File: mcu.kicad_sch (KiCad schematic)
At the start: 50 parts, among them IC3 RP2040, U1 W25Q64JVSSIQ, Y1 ABM3B-12.000MHZ-10-1-U-T

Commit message: reannotate
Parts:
- renumbered TP30 to TP28, TP31 to TP29, TP32 to TP30, TP33 to TP31, TP34 to TP32, TP37 to TP33, TP50 to TP34, TP51 to TP35, TP35 to TP36, TP36 to TP37
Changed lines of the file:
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@@
   (symbol (lib_id "Connector:TestPoint_Small") (at 198.12 133.35 0) (unit 1)
     (in_bom yes) (on_board yes) (dnp no)
-    (property "Reference" "TP33" (at 198.755 132.08 0)
+    (property "Reference" "TP31" (at 198.755 132.08 0)
       (effects (font (size 1.27 1.27)) (justify left) hide)
     )
@@
       (project "gkos_pebble"
         (path "/ab6fff6e-44fa-4992-ab9d-8d9a7df4367d/b094ad32-9f85-443d-ad4d-e6b703944261"
-          (reference "TP33") (unit 1)
+          (reference "TP31") (unit 1)
         )
       )
@@
   (symbol (lib_id "Connector:TestPoint_Small") (at 198.12 156.21 0) (unit 1)
     (in_bom yes) (on_board yes) (dnp no)
-    (property "Reference" "TP35" (at 198.755 154.94 0)
+    (property "Reference" "TP36" (at 198.755 154.94 0)
       (effects (font (size 1.27 1.27)) (justify left) hide)
     )
@@
       (project "gkos_pebble"
         (path "/ab6fff6e-44fa-4992-ab9d-8d9a7df4367d/b094ad32-9f85-443d-ad4d-e6b703944261"
-          (reference "TP35") (unit 1)
+          (reference "TP36") (unit 1)
         )
       )
@@
   (symbol (lib_id "Connector:TestPoint_Small") (at 198.12 148.59 0) (unit 1)
     (in_bom yes) (on_board yes) (dnp no)
-    (property "Reference" "TP37" (at 198.755 147.32 0)
+    (property "Reference" "TP33" (at 198.755 147.32 0)
       (effects (font (size 1.27 1.27)) (justify left) hide)
     )
@@
       (project "gkos_pebble"
         (path "/ab6fff6e-44fa-4992-ab9d-8d9a7df4367d/b094ad32-9f85-443d-ad4d-e6b703944261"
-          (reference "TP37") (unit 1)
+          (reference "TP33") (unit 1)
         )
       )
@@
   (symbol (lib_id "Connector:TestPoint_Small") (at 198.12 135.89 0) (unit 1)
     (in_bom yes) (on_board yes) (dnp no)
-    (property "Reference" "TP34" (at 198.755 134.62 0)
+    (property "Reference" "TP32" (at 198.755 134.62 0)
       (effects (font (size 1.27 1.27)) (justify left) hide)
     )
@@
       (project "gkos_pebble"
         (path "/ab6fff6e-44fa-4992-ab9d-8d9a7df4367d/b094ad32-9f85-443d-ad4d-e6b703944261"
-          (reference "TP34") (unit 1)
+          (reference "TP32") (unit 1)
         )
       )
@@
   (symbol (lib_id "Connector:TestPoint_Small") (at 162.56 57.15 0) (unit 1)
     (in_bom yes) (on_board yes) (dnp no)
-    (property "Reference" "TP32" (at 163.195 55.88 0)
+    (property "Reference" "TP30" (at 163.195 55.88 0)
       (effects (font (size 1.27 1.27)) (justify left))
     )
@@
       (project "gkos_pebble"
         (path "/ab6fff6e-44fa-4992-ab9d-8d9a7df4367d/b094ad32-9f85-443d-ad4d-e6b703944261"
-          (reference "TP32") (unit 1)
+          (reference "TP30") (unit 1)
         )
       )
@@
   (symbol (lib_id "Connector:TestPoint_Small") (at 198.12 153.67 0) (unit 1)
     (in_bom yes) (on_board yes) (dnp no)
-    (property "Reference" "TP51" (at 198.755 152.4 0)
+    (property "Reference" "TP35" (at 198.755 152.4 0)
       (effects (font (size 1.27 1.27)) (justify left) hide)
     )
@@
       (project "gkos_pebble"
         (path "/ab6fff6e-44fa-4992-ab9d-8d9a7df4367d/b094ad32-9f85-443d-ad4d-e6b703944261"
-          (reference "TP51") (unit 1)
+          (reference "TP35") (unit 1)
         )
       )
@@
   (symbol (lib_id "Connector:TestPoint_Small") (at 198.12 158.75 0) (unit 1)
     (in_bom yes) (on_board yes) (dnp no)
-    (property "Reference" "TP36" (at 198.755 157.48 0)
+    (property "Reference" "TP37" (at 198.755 157.48 0)
       (effects (font (size 1.27 1.27)) (justify left) hide)
     )
@@
       (project "gkos_pebble"
         (path "/ab6fff6e-44fa-4992-ab9d-8d9a7df4367d/b094ad32-9f85-443d-ad4d-e6b703944261"
-          (reference "TP36") (unit 1)
+          (reference "TP37") (unit 1)
         )
       )
@@
   (symbol (lib_id "Connector:TestPoint_Small") (at 53.34 135.89 0) (unit 1)
     (in_bom yes) (on_board yes) (dnp no)
-    (property "Reference" "TP30" (at 53.975 134.62 0)
+    (property "Reference" "TP28" (at 53.975 134.62 0)
       (effects (font (size 1.27 1.27)) (justify left) hide)
     )
@@
       (project "gkos_pebble"
         (path "/ab6fff6e-44fa-4992-ab9d-8d9a7df4367d/b094ad32-9f85-443d-ad4d-e6b703944261"
-          (reference "TP30") (unit 1)
+          (reference "TP28") (unit 1)
         )
       )
@@
   (symbol (lib_id "Connector:TestPoint_Small") (at 198.12 151.13 0) (unit 1)
     (in_bom yes) (on_board yes) (dnp no)
-    (property "Reference" "TP50" (at 198.755 149.86 0)
+    (property "Reference" "TP34" (at 198.755 149.86 0)
       (effects (font (size 1.27 1.27)) (justify left) hide)
     )
@@
       (project "gkos_pebble"
         (path "/ab6fff6e-44fa-4992-ab9d-8d9a7df4367d/b094ad32-9f85-443d-ad4d-e6b703944261"
-          (reference "TP50") (unit 1)
+          (reference "TP34") (unit 1)
         )
       )
@@
   (symbol (lib_id "Connector:TestPoint_Small") (at 53.34 163.83 0) (mirror x) (unit 1)
     (in_bom yes) (on_board yes) (dnp no)
-    (property "Reference" "TP31" (at 53.975 165.1 0)
+    (property "Reference" "TP29" (at 53.975 165.1 0)
       (effects (font (size 1.27 1.27)) (justify left) hide)
     )
@@
       (project "gkos_pebble"
         (path "/ab6fff6e-44fa-4992-ab9d-8d9a7df4367d/b094ad32-9f85-443d-ad4d-e6b703944261"
-          (reference "TP31") (unit 1)
-        )
-      )
+          (reference "TP29") (unit 1)
+        )
+      )

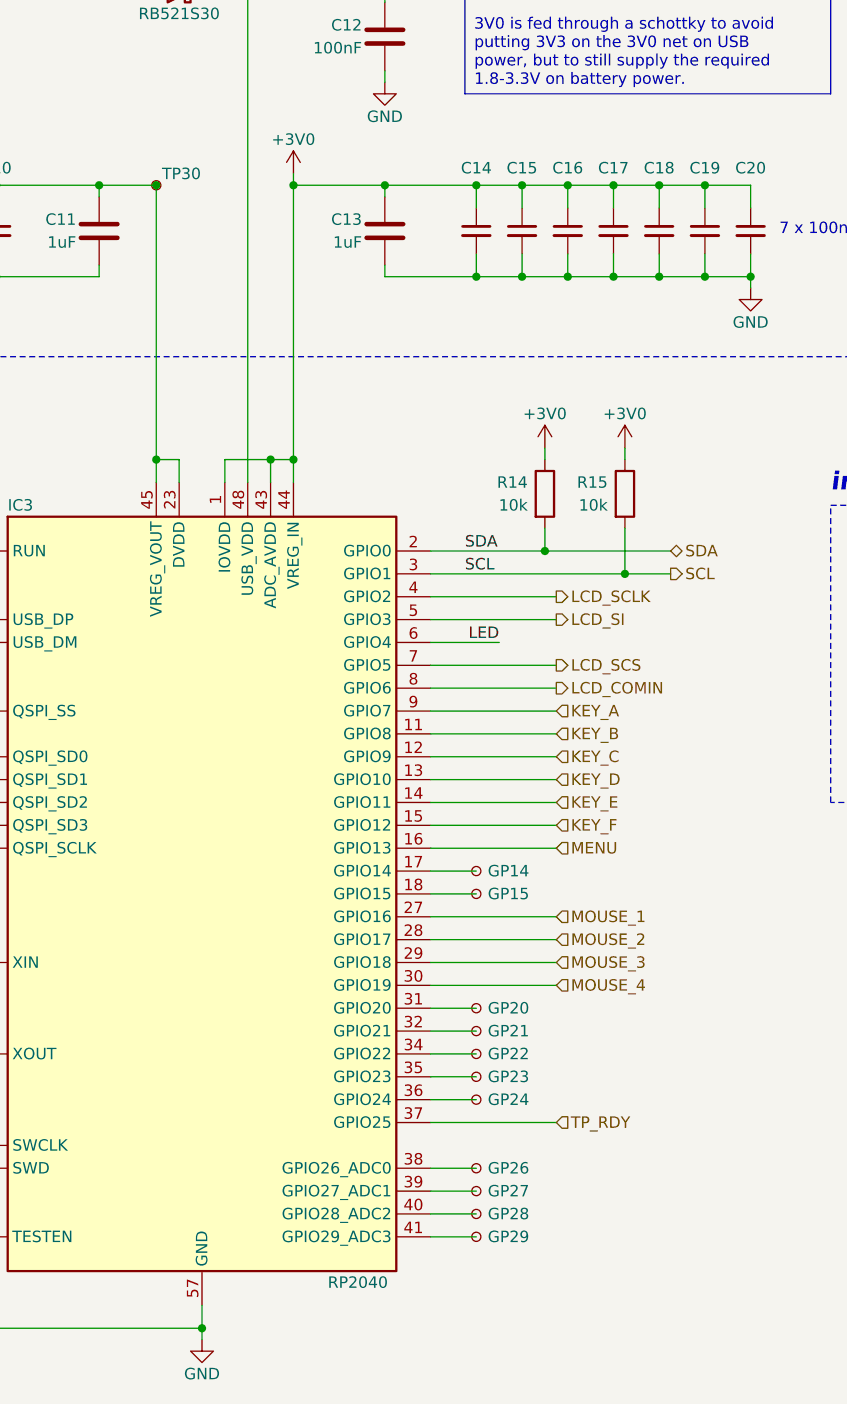
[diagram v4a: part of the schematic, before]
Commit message: GPIO shuffling
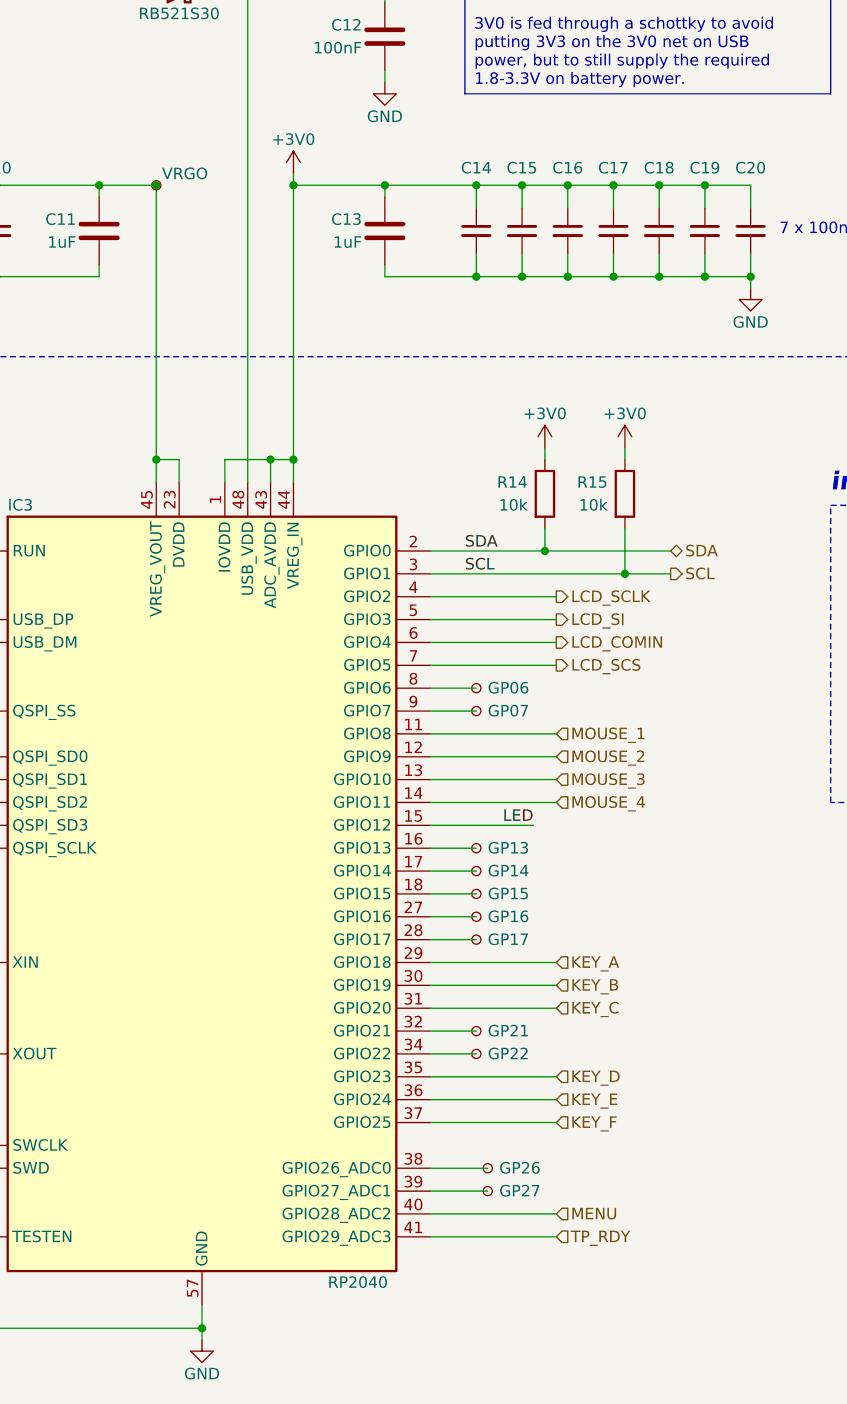
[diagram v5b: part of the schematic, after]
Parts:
- TP30: value TestPoint_Small -> VRGO
- TP31: value GP14 -> GP06
- TP32: value GP15 -> GP07
- TP33: value GP20 -> GP13
- TP34: value GP21 -> GP14
- TP35: value GP22 -> GP15
- TP36: value GP23 -> GP16
- TP37: value GP24 -> GP17
- TP38: value GP26 -> GP21
- TP39: value GP27 -> GP22
- TP40: value GP28 -> GP26
- TP41: value GP29 -> GP27
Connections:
- net KEY_A: now also IC3.29 (GPIO18); no longer IC3.9 (GPIO7)
- net KEY_B: now also IC3.30 (GPIO19); no longer IC3.11 (GPIO8)
- net KEY_C: now also IC3.31 (GPIO20); no longer IC3.12 (GPIO9)
- net KEY_D: now also IC3.35 (GPIO23); no longer IC3.13 (GPIO10)
- net KEY_E: now also IC3.36 (GPIO24); no longer IC3.14 (GPIO11)
- net KEY_F: now also IC3.37 (GPIO25); no longer IC3.15 (GPIO12)
- net LCD_COMIN: now also IC3.6 (GPIO4); no longer IC3.8 (GPIO6)
- net LED: now also IC3.15 (GPIO12); no longer IC3.6 (GPIO4)
- net MENU: now also IC3.40 (GPIO28_ADC2); no longer IC3.16 (GPIO13)
- net MOUSE_1: now also IC3.11 (GPIO8); no longer IC3.27 (GPIO16)
- net MOUSE_2: now also IC3.12 (GPIO9); no longer IC3.28 (GPIO17)
- net MOUSE_3: now also IC3.13 (GPIO10); no longer IC3.29 (GPIO18)
- net MOUSE_4: now also IC3.14 (GPIO11); no longer IC3.30 (GPIO19)
- net TP_RDY: now also IC3.41 (GPIO29_ADC3); no longer IC3.37 (GPIO25)
- net at IC3.38 (GPIO26_ADC0): now also TP40.1; no longer TP38.1
- net at IC3.17 (GPIO14): now also TP34.1; no longer TP31.1
- net at TP36.1: now also IC3.27 (GPIO16); no longer IC3.35 (GPIO23)
- net at TP33.1: now also IC3.16 (GPIO13); no longer IC3.31 (GPIO20)
- net at IC3.18 (GPIO15): now also TP35.1; no longer TP32.1
- net at IC3.39 (GPIO27_ADC1): now also TP41.1; no longer TP39.1
- net at IC3.34 (GPIO22): now also TP39.1; no longer TP35.1
- net at IC3.32 (GPIO21): now also TP38.1; no longer TP34.1
- net at TP37.1: now also IC3.28 (GPIO17); no longer IC3.36 (GPIO24)
- new net: IC3.8 (GPIO6), TP31.1
- new net: IC3.9 (GPIO7), TP32.1

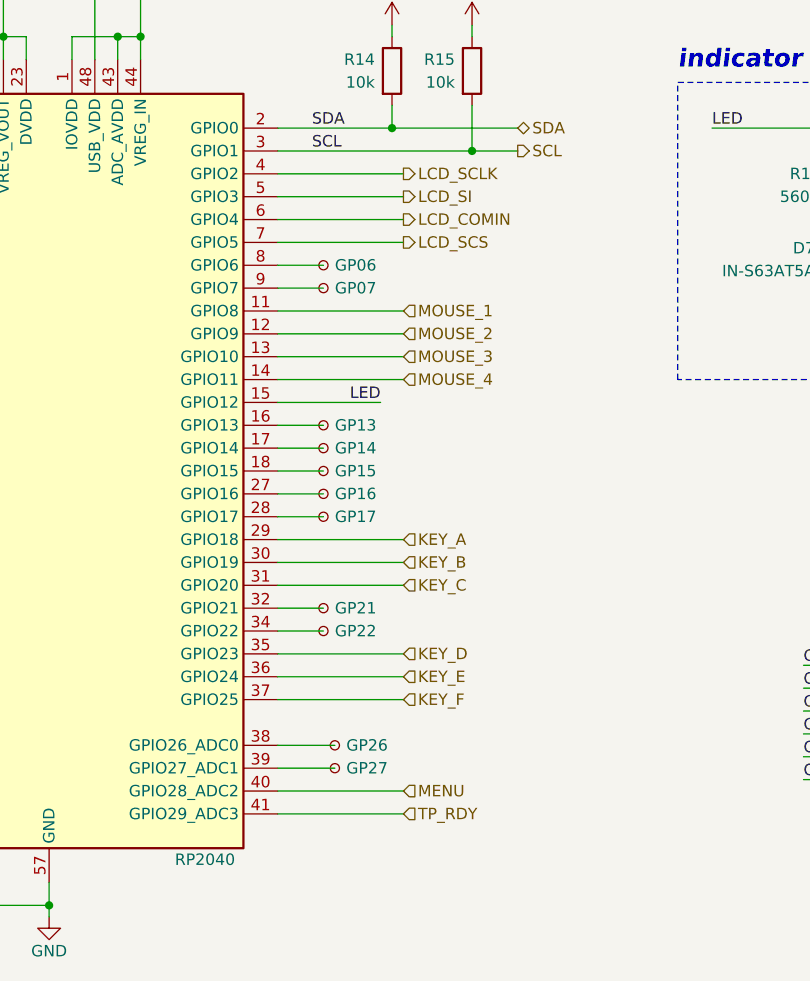
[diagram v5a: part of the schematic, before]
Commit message: GPIO shuffling + reannotate
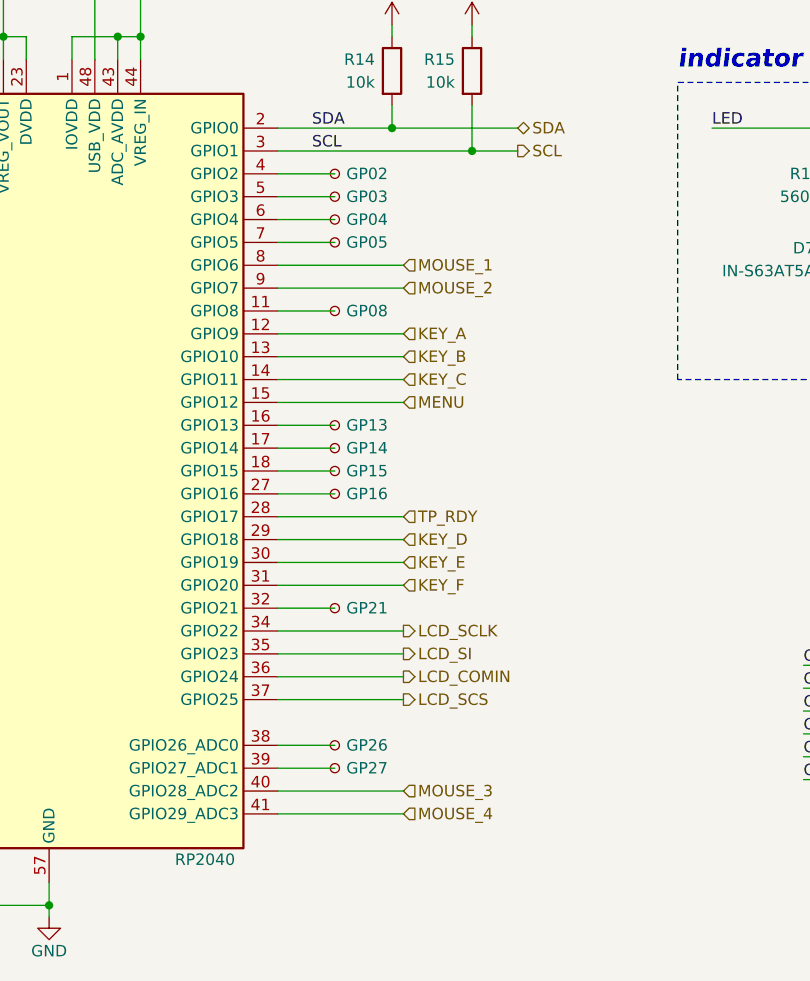
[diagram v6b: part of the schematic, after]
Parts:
- added TP42: GP27, TestPoint:TestPoint_Pad_D2.0mm, symbol Connector:TestPoint_Small
- TP31: value GP06 -> GP02
- TP32: value GP07 -> GP03
- TP33: value GP13 -> GP04
- TP34: value GP14 -> GP05
- TP35: value GP15 -> GP08
- TP36: value GP16 -> GP13
- TP37: value GP17 -> GP14
- TP38: value GP21 -> GP15
- TP39: value GP22 -> GP16
- TP40: value GP26 -> GP21
- TP41: value GP27 -> GP26
- renumbered TP42 to TP43, TP43 to TP44, TP44 to TP45, TP45 to TP46, TP46 to TP47, TP47 to TP48
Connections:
- net KEY_A: now also IC3.12 (GPIO9); no longer IC3.29 (GPIO18)
- net KEY_B: now also IC3.13 (GPIO10); no longer IC3.30 (GPIO19)
- net KEY_C: now also IC3.14 (GPIO11); no longer IC3.31 (GPIO20)
- net KEY_D: now also IC3.29 (GPIO18); no longer IC3.35 (GPIO23)
- net KEY_E: now also IC3.30 (GPIO19); no longer IC3.36 (GPIO24)
- net KEY_F: now also IC3.31 (GPIO20); no longer IC3.37 (GPIO25)
- net LCD_COMIN: now also IC3.36 (GPIO24); no longer IC3.6 (GPIO4)
- net LCD_SCLK: now also IC3.34 (GPIO22); no longer IC3.4 (GPIO2)
- net LCD_SCS: now also IC3.37 (GPIO25); no longer IC3.7 (GPIO5)
- net LCD_SI: now also IC3.35 (GPIO23); no longer IC3.5 (GPIO3)
- net LED: no longer IC3.15 (GPIO12)
- net MENU: now also IC3.15 (GPIO12); no longer IC3.40 (GPIO28_ADC2)
- net MOUSE_1: now also IC3.8 (GPIO6); no longer IC3.11 (GPIO8)
- net MOUSE_2: now also IC3.9 (GPIO7); no longer IC3.12 (GPIO9)
- net MOUSE_3: now also IC3.40 (GPIO28_ADC2); no longer IC3.13 (GPIO10)
- net MOUSE_4: now also IC3.41 (GPIO29_ADC3); no longer IC3.14 (GPIO11)
- net TP_RDY: now also IC3.28 (GPIO17); no longer IC3.41 (GPIO29_ADC3)
- net at TP40.1: now also IC3.32 (GPIO21); no longer IC3.38 (GPIO26_ADC0)
- net at IC3.16 (GPIO13): now also TP36.1; no longer TP33.1
- net at IC3.39 (GPIO27_ADC1): now also TP42.1; no longer TP41.1
- net at TP35.1: now also IC3.11 (GPIO8); no longer IC3.18 (GPIO15)
- net at TP39.1: now also IC3.27 (GPIO16); no longer IC3.34 (GPIO22)
- net at IC3.17 (GPIO14): now also TP37.1; no longer TP34.1
- net at TP38.1: now also IC3.18 (GPIO15); no longer IC3.32 (GPIO21)
- net at TP31.1: now also IC3.4 (GPIO2); no longer IC3.8 (GPIO6)
- net at TP32.1: now also IC3.5 (GPIO3); no longer IC3.9 (GPIO7)
- new net: IC3.38 (GPIO26_ADC0), TP41.1
- new net: IC3.6 (GPIO4), TP33.1
- new net: IC3.7 (GPIO5), TP34.1

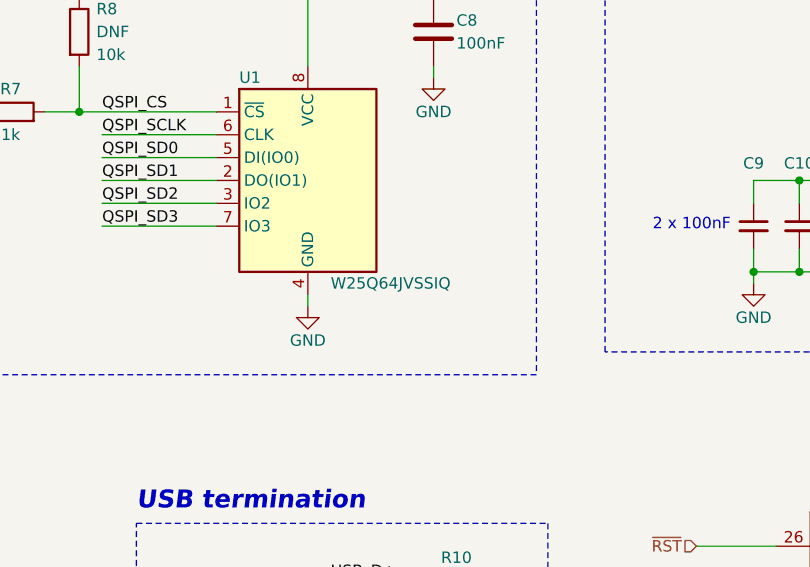
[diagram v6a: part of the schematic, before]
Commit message: swap flash to smaller WSON package
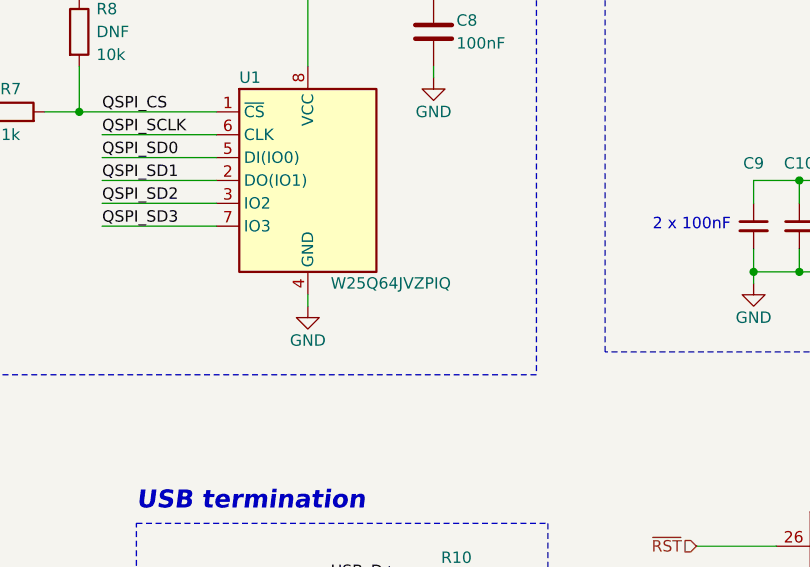
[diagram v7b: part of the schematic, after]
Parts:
- U1: value W25Q64JVSSIQ -> W25Q64JVZPIQ; footprint Package_SO:SOIC-8_5.23x5.23mm_P1.27mm -> Package_SON:WSON-8-1EP_6x5mm_P1.27mm_EP3.4x4.3mm
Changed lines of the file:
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@@
       (effects (font (size 1.27 1.27)) (justify left))
     )
-    (property "Value" "W25Q64JVSSIQ" (at 92.71 68.58 0)
+    (property "Value" "W25Q64JVZPIQ" (at 92.71 68.58 0)
       (effects (font (size 1.27 1.27)) (justify left))
     )
-    (property "Footprint" "Package_SO:SOIC-8_5.23x5.23mm_P1.27mm" (at 90.17 57.15 0)
+    (property "Footprint" "Package_SON:WSON-8-1EP_6x5mm_P1.27mm_EP3.4x4.3mm" (at 90.17 57.15 0)
       (effects (font (size 1.27 1.27)) hide)
     )
